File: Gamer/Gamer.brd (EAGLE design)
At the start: 168.9 x 63.5 mm, 44 parts, among them J1 HEADER-1X8, J2 HEADER-1X8, J3 HEADER-1X8, J4 HEADER-1X8, J5 HEADER-1X8, J6 HEADER-1X8, J7 HEADER-1X8, J8 HEADER-1X8, U1 MMA8653FCR1, U2 ATTINY48, U3 ULN2803AFWG, U4 ATTINY48, U5 ULN2803AFWG, U6 ATTINY48, U7 ULN2803AFWG, U8 ATTINY48, U9 ULN2803AFWG

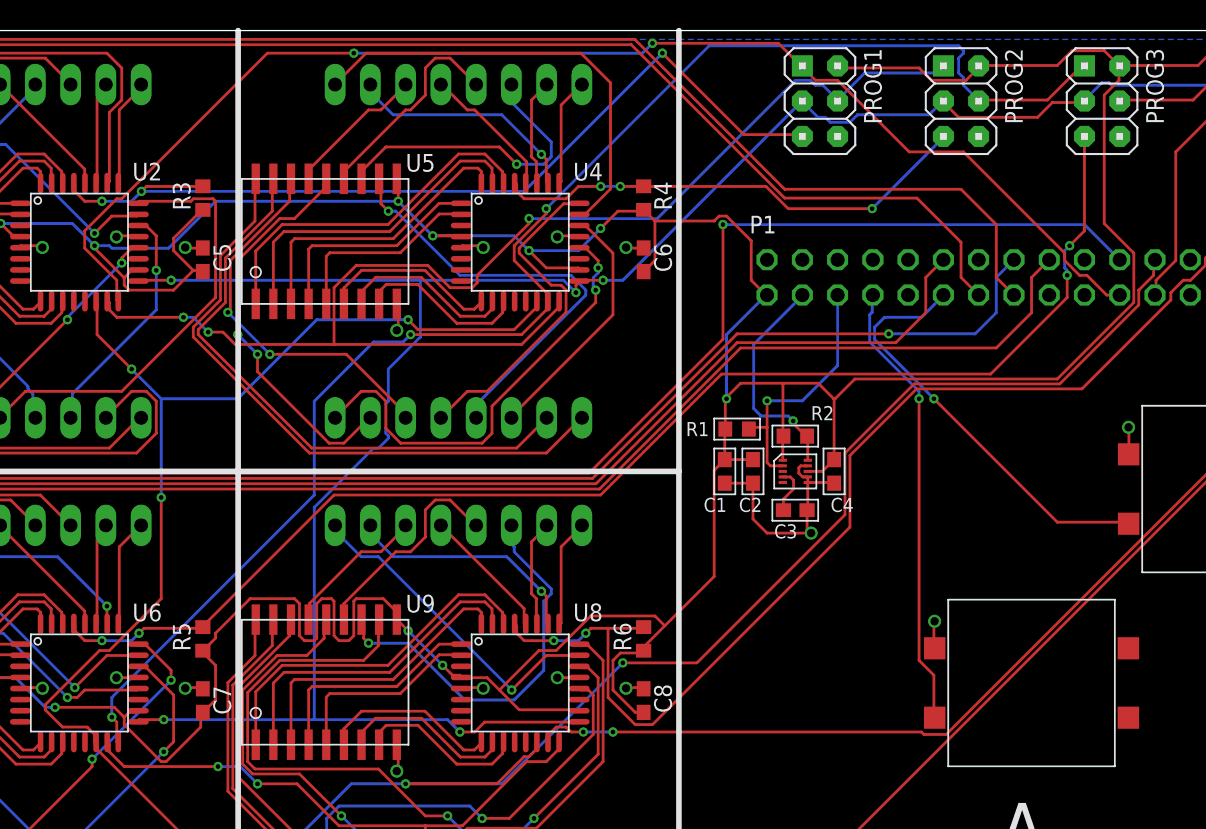
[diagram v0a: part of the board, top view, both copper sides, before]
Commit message: gamer - Order of SPI chain was backwards
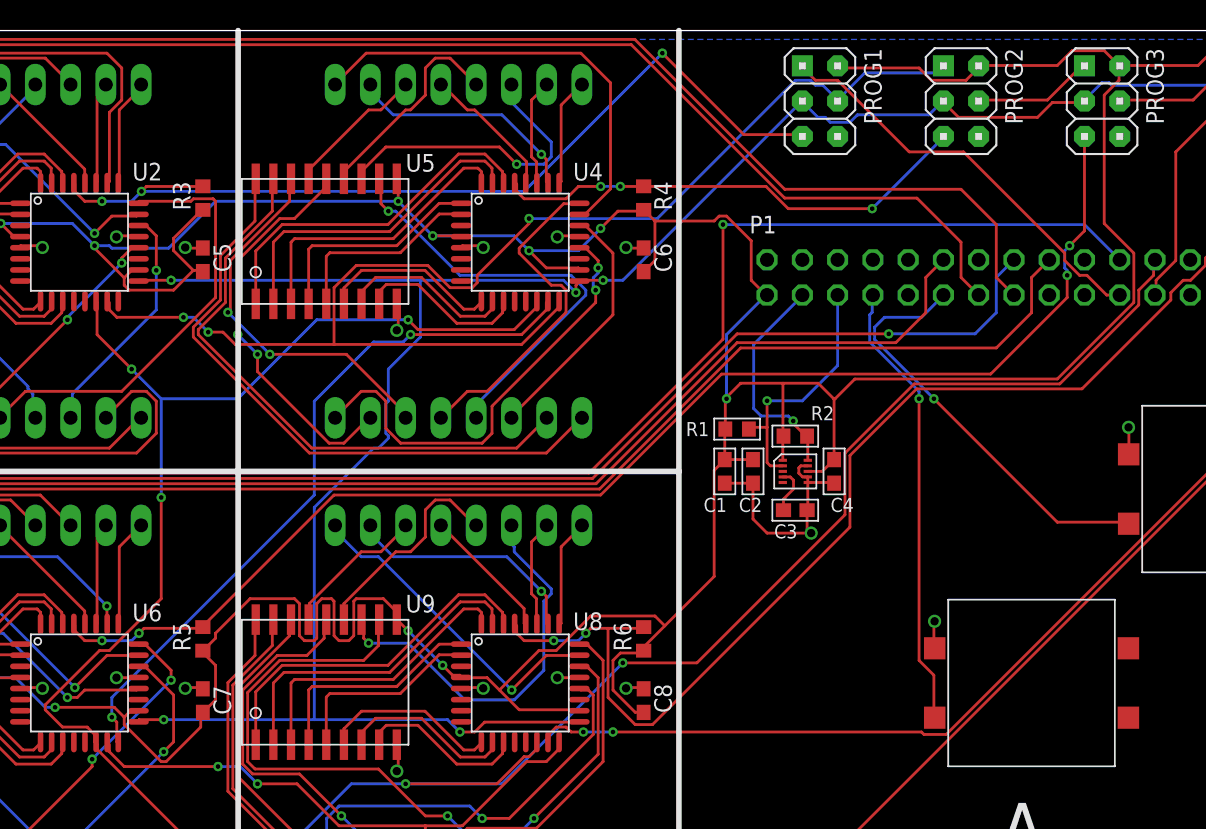
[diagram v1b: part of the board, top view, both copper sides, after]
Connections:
- removed net 10/MISO: PROG4.4, U8.PB3
- removed net MOSI1/MISO2: PROG1.4, PROG2.1, U2.PB3, U4.PB4
- removed net MOSI2/MISO3: PROG2.4, PROG3.1, U4.PB3, U6.PB4
- removed net MOSI3/MISO4: PROG3.4, PROG4.1, U6.PB3, U8.PB4
- new net S2IN: PROG1.1, PROG2.4, U2.PB4, U4.PB3
- new net S3IN: PROG2.1, PROG3.4, U4.PB4, U6.PB3
- new net S4IN: PROG3.1, PROG4.4, U6.PB4, U8.PB3
- net 10/MOSI: now also PROG1.4, U2.PB3
- net 9/MISO: now also PROG4.1, U8.PB4; no longer PROG1.1, U2.PB4
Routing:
- net MOSI3/MISO4: track 154.7 -> 0.00 mm, vias 2 -> 0
- net S4IN: track 0.00 -> 144.0 mm, vias 0 -> 4
- net MOSI2/MISO3: track 107.8 -> 0.00 mm, vias 3 -> 0
- net MOSI1/MISO2: track 93.4 -> 0.00 mm, vias 3 -> 0
- net S3IN: track 0.00 -> 93.1 mm, vias 0 -> 3
- net 9/MISO: track 94.1 -> 184.2 mm
- net 10/MISO: track 84.7 -> 0.00 mm, vias 2 -> 0

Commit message: gamer - ERC passes (with many okay warnings)
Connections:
- net 3V3 renamed VCC
- removed net N$1: START.4
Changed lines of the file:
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@@
 <wire x1="58.293" y1="16.129" x2="63.627" y2="16.891" width="0" layer="19" extent="1-1"/>
 </signal>
-<signal name="3V3">
+<signal name="VCC">
 <contactref element="C2" pad="1"/>
 <contactref element="C1" pad="1"/>
@@
 <wire x1="77.8764" y1="30.0482" x2="94.7674" y2="12.8016" width="0" layer="19" extent="1-16"/>
 </signal>
-<signal name="N$1">
-<contactref element="START" pad="4"/>
-</signal>
 <signal name="S2IN">

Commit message: gamer - Rerouted 100%
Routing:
- net 10/MOSI: track 0.00 -> 89.0 mm, vias 0 -> 3
- net 9/MISO: track 184.2 -> 107.3 mm
- net S2IN: track 0.00 -> 76.1 mm, vias 0 -> 3
- net 8/CE0: track 183.5 -> 159.7 mm, vias 6 -> 5
- net M4_COL7: track 37.7 -> 20.1 mm
- net M1_ROW1: track 17.3 -> 34.1 mm, vias 1 -> 0
- net S3IN: track 93.1 -> 109.1 mm, vias 3 -> 4
- net M4_ROW1: track 17.3 -> 31.8 mm, vias 1 -> 0
- net VCC: track 328.0 -> 342.1 mm, vias 13 -> 14
- net M4_COL6: track 29.0 -> 17.4 mm
- net M2_ROW0: track 32.6 -> 22.9 mm, vias 2 -> 1
- net M3_ROW3: track 21.8 -> 31.2 mm, vias 2 -> 0
- net M4_COL4: track 26.8 -> 18.6 mm
- net M1_ROW0: track 25.6 -> 33.2 mm, vias 2 -> 1
- net M2_COL6: track 22.1 -> 14.5 mm
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
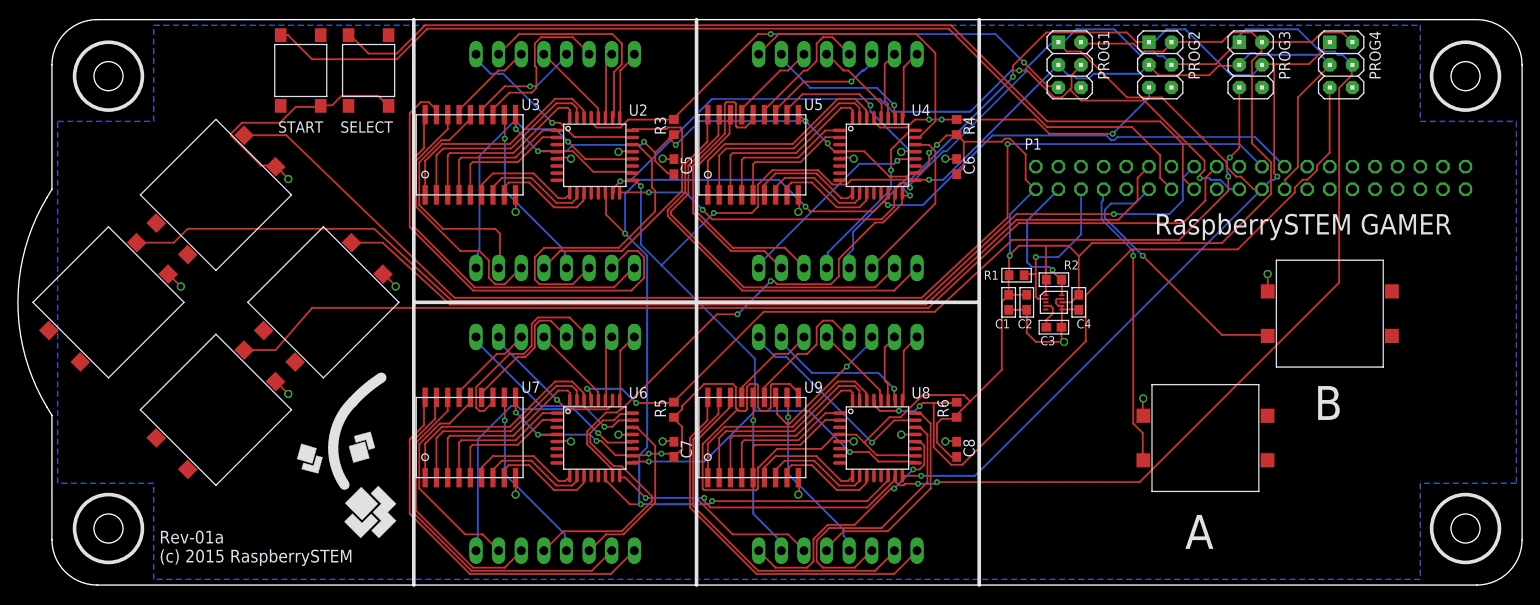
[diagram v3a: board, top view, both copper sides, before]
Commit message: gamer - main header was flipped.  Flipped and rerouted 100%.
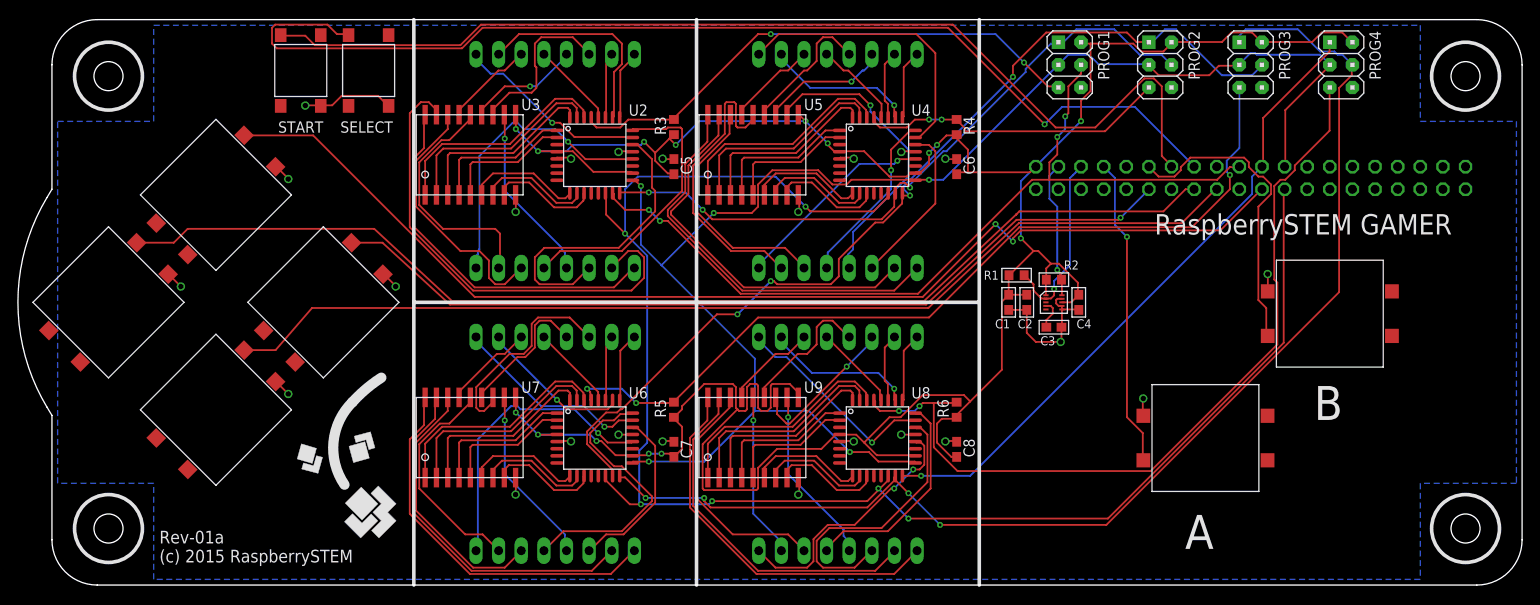
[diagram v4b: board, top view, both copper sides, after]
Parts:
- flipped P1 to the bottom, turned to 180 degrees
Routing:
- net 9/MISO: track 107.3 -> 73.0 mm, vias 2 -> 1
- net VCC: track 342.1 -> 308.9 mm, vias 14 -> 15
- net 8/CE0: track 159.7 -> 182.7 mm, vias 5 -> 6
- net 22: track 107.0 -> 123.9 mm, vias 0 -> 1
- net GND: track 82.0 -> 65.2 mm, vias 23 -> 24
- net M4_RESET: track 86.2 -> 93.0 mm
- net 10/MOSI: track 89.0 -> 95.7 mm, vias 3 -> 4
- net 25: track 134.6 -> 128.7 mm, vias 1 -> 2
- net 27: track 111.5 -> 117.3 mm
- net S4IN: track 143.5 -> 139.2 mm
- net 17/RTS: track 30.6 -> 34.9 mm, vias 1 -> 0
- net 11/SCLK: track 175.3 -> 172.4 mm
- net 23: track 130.2 -> 127.7 mm, vias 1 -> 0
- net 4: track 32.5 -> 35.0 mm
- net 24: track 119.3 -> 116.8 mm
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
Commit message: gamer - first new protoype fixes... Unrouted.
- RaspberrySTEM GAMER name obscured by header
- mounting holes
- header pins flipped
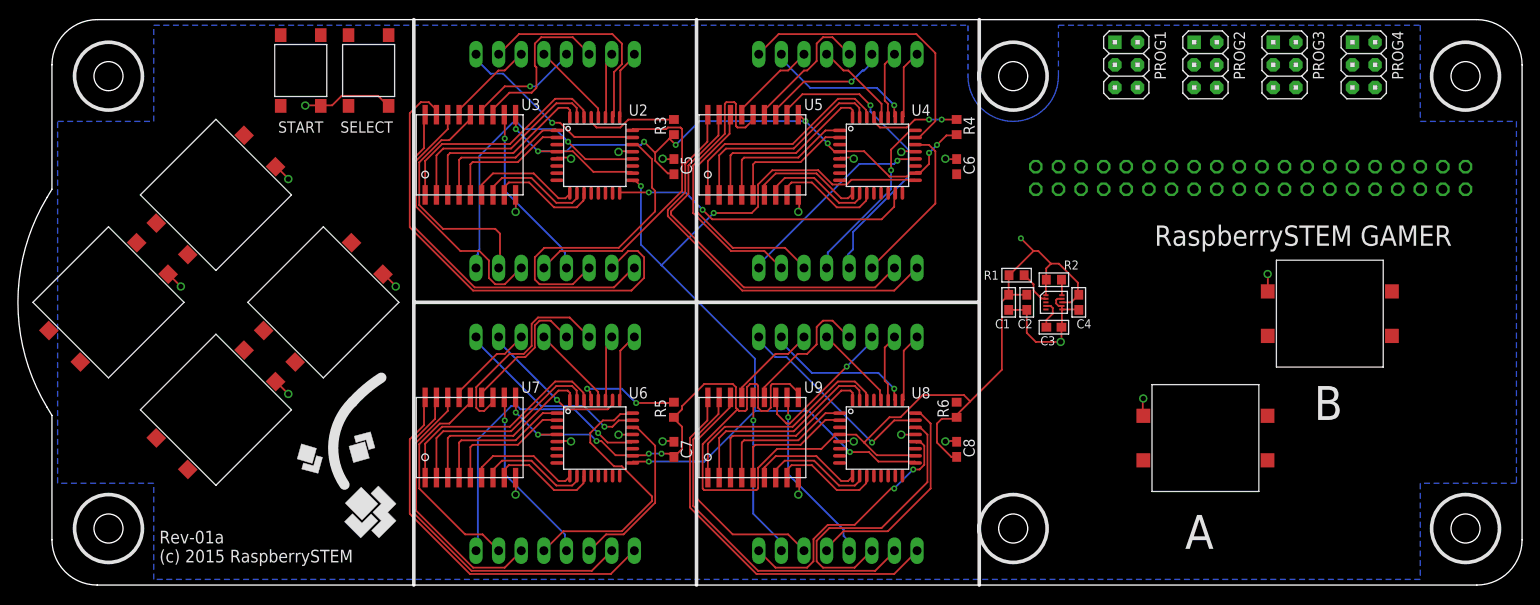
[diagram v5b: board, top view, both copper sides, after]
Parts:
- moved PROG1 6.35 mm to (120.7, 58.4)
- moved PROG2 5.08 mm to (129.5, 58.4)
- moved PROG3 3.81 mm to (138.4, 58.4)
- moved PROG4 2.54 mm to (147.3, 58.4)
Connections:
- net 10/MOSI: now also P1.20; no longer P1.19
- net 11/SCLK: now also P1.24; no longer P1.23
- net 12: now also P1.31; no longer P1.32
- net 13: now also P1.34; no longer P1.33
- net 14/TX: now also P1.7; no longer P1.8
- net 15/RX: now also P1.9; no longer P1.10
- net 16: now also P1.35; no longer P1.36
- net 17/RTS: now also P1.12; no longer P1.11
- net 18: now also P1.11; no longer P1.12
- net 19: now also P1.36; no longer P1.35
- net 2/SDA: now also P1.4; no longer P1.3
- net 20: now also P1.37; no longer P1.38
- net 21: now also P1.39; no longer P1.40
- net 22: now also P1.16; no longer P1.15
- net 23: now also P1.15; no longer P1.16
- net 24: now also P1.17; no longer P1.18
- net 25: now also P1.21; no longer P1.22
- net 26: now also P1.38; no longer P1.37
- net 27: now also P1.14; no longer P1.13
- net 3/SCL: now also P1.6; no longer P1.5
- net 3V3_2: now also P1.18; no longer P1.17
- net 4: now also P1.8; no longer P1.7
- net 5: now also P1.30; no longer P1.29
- net 5V_1: now also P1.3; no longer P1.4
- net 5V_2: now also P1.1; no longer P1.2
- net 6: now also P1.32; no longer P1.31
- net 7/CE1: now also P1.25; no longer P1.26
- net 8/CE0: now also P1.23; no longer P1.24
- net 9/MISO: now also P1.22; no longer P1.21
- net GND: now also P1.10; no longer P1.9
- net GND2: now also P1.26; no longer P1.25
- net GND3: now also P1.19; no longer P1.20
- net GND4: now also P1.13; no longer P1.14
- net GND5: now also P1.5; no longer P1.6
- net GND6: now also P1.40; no longer P1.39
- net GND7: now also P1.33; no longer P1.34
- net GND8: now also P1.29; no longer P1.30
- net ID1: now also P1.28; no longer P1.27
- net ID2: now also P1.27; no longer P1.28
- net VCC: now also P1.2; no longer P1.1
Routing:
- net 8/CE0: track 182.7 -> 0.00 mm, vias 6 -> 0
- net S4IN: track 139.2 -> 0.00 mm, vias 4 -> 0
- net 25: track 128.7 -> 0.00 mm, vias 2 -> 0
- net 23: track 127.7 -> 0.00 mm
- net 22: track 123.9 -> 0.00 mm, vias 1 -> 0
- net 27: track 117.3 -> 0.00 mm
- net 24: track 116.8 -> 0.00 mm
- net S3IN: track 109.1 -> 0.00 mm, vias 4 -> 0
- net 18: track 97.5 -> 0.00 mm, vias 1 -> 0
- net 10/MOSI: track 95.7 -> 0.00 mm, vias 4 -> 0
- net M4_RESET: track 93.0 -> 0.00 mm, vias 2 -> 0
- net M3_RESET: track 96.5 -> 11.9 mm, vias 3 -> 2
- net 9/MISO: track 73.0 -> 0.00 mm, vias 1 -> 0
- net VCC: track 308.9 -> 236.4 mm, vias 15 -> 14
- net 11/SCLK: track 172.4 -> 103.8 mm, vias 5 -> 4
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
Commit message: gamer - rerouted.  remasked mounting holes around bottom gnd plane
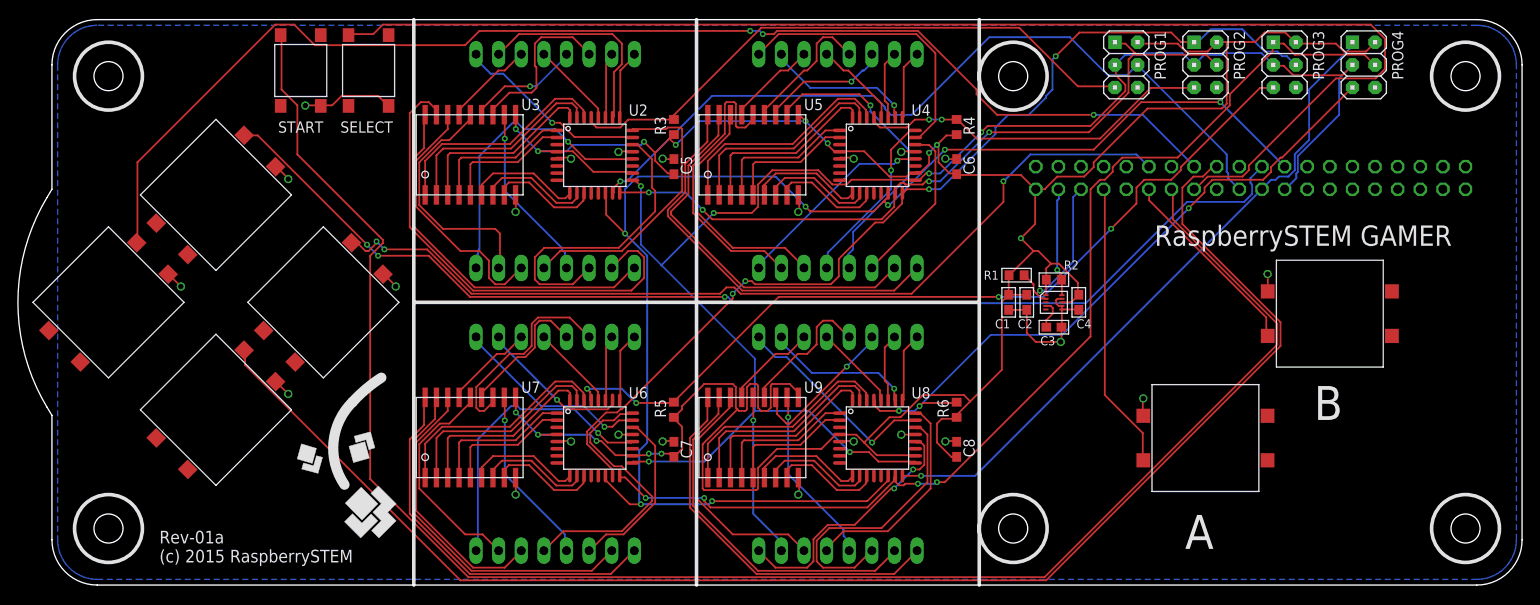
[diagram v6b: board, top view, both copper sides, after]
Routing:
- net 27: track 0.00 -> 194.9 mm
- net 24: track 0.00 -> 166.1 mm
- net 8/CE0: track 0.00 -> 163.1 mm, vias 0 -> 7
- net 22: track 0.00 -> 148.3 mm
- net 23: track 0.00 -> 142.7 mm, vias 0 -> 3
- net 25: track 0.00 -> 129.8 mm, vias 0 -> 3
- net S4IN: track 0.00 -> 122.1 mm, vias 0 -> 4
- net S3IN: track 0.00 -> 111.9 mm, vias 0 -> 4
- net 18: track 0.00 -> 101.9 mm, vias 0 -> 3
- net 10/MOSI: track 0.00 -> 89.3 mm, vias 0 -> 1
- net M3_RESET: track 11.9 -> 95.2 mm, vias 2 -> 4
- net VCC: track 236.4 -> 319.0 mm
- net 11/SCLK: track 103.8 -> 181.9 mm, vias 4 -> 6
- net 9/MISO: track 0.00 -> 75.4 mm, vias 0 -> 1
- net M4_RESET: track 0.00 -> 74.6 mm, vias 0 -> 3
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- added copper zone on layer 16, net N$1
- removed copper zone on layer 16, net GND

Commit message: gamer - rev up, added accel silkscreen, other fixes
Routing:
- net 10/MOSI: track 89.3 -> 124.8 mm
- net S3IN: track 111.9 -> 108.5 mm, vias 4 -> 3
- added copper zone on layer 16, net GND
- removed copper zone on layer 16, net N$1
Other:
- board text added: "Rev-01b (c) 2015 RaspberrySTEM"
- board text added: "X"
- board text added: "Y"
- board text added: "Z"
- board text removed: "Rev-01a (c) 2015 RaspberrySTEM"

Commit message: gamer - updated BOM and silkscreen
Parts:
- renumbered A to B7, B to B8, DOWN to B6, LEFT to B4, P1 to J9, RIGHT to B5, SELECT to B2, START to B1, UP to B3
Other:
- board text added: "A"
- board text added: "B"
- board text added: "SELECT"
- board text added: "START"
